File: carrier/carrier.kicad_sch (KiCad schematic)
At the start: 2 parts, among them J1 DF40GB-30DP-0.4V(51), U1 TC58NVG1S3HBAI6

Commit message: Rename project libraries to 'carrier' for consistency
lib/bga67-to-dip.kicad_sym -> lib/carrier.kicad_sym; nicknames now match
the directory names. Schematic instance lib_ids and U1's footprint field
updated. Both projects' lib tables rebuilt.

Co-Authored-By: Claude Opus 5 <noreply@anthropic.com>
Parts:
- J1: symbol bga67-to-dip:DF40GB-30DP-0.4V_51_ -> carrier:DF40GB-30DP-0.4V_51_
- U1: footprint bga67-to-dip:BGA-67_6.5x8.0mm_Layout8x10_P0.8mm -> carrier:BGA-67_6.5x8.0mm_Layout8x10_P0.8mm; symbol bga67-to-dip:TC58NVG1S3HBAI6 -> carrier:TC58NVG1S3HBAI6
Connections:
- net ALE: no longer J1.12, U1.B3 (ALE)
- net CLE: no longer J1.8, U1.C4 (CLE)
- net GND: no longer J1.10, J1.11, J1.14, J1.18, J1.2, J1.22, J1.23, J1.26, J1.27, J1.3, J1.30, J1.6, J1.7, J1.G1 (GND), J1.G2 (GND), J1.G3 (GND), J1.G4 (GND), U1.B4 (VSS), U1.J2 (VSS), U1.J7 (VSS)
- net IO1: no longer J1.1, U1.G3 (I/O1)
- net IO2: no longer J1.5, U1.H3 (I/O2)
- net IO3: no longer J1.9, U1.J3 (I/O3)
- net IO4: no longer J1.13, U1.J4 (I/O4)
- net IO5: no longer J1.17, U1.J5 (I/O5)
- net IO6: no longer J1.21, U1.H6 (I/O6)
- net IO7: no longer J1.25, U1.J6 (I/O7)
- net IO8: no longer J1.29, U1.H7 (I/O8)
- net RY//BY: no longer J1.28, U1.B7 (RY/~{BY})
- net VCC: no longer J1.15, J1.19, U1.G7 (VCC), U1.H5 (VCC)
- net /CE: no longer J1.4, U1.B5 (~{CE})
- net /RE: no longer J1.20, U1.C3 (~{RE})
- net /WE: no longer J1.16, U1.B6 (~{WE})
- net /WP: no longer J1.24, U1.B2 (~{WP})
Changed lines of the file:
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@@
 	)
 	(symbol
-		(lib_id "bga67-to-dip:DF40GB-30DP-0.4V_51_")
+		(lib_id "carrier:DF40GB-30DP-0.4V_51_")
 		(at 170.18 92.71 0)
 		(unit 1)
@@
 	)
 	(symbol
-		(lib_id "bga67-to-dip:TC58NVG1S3HBAI6")
+		(lib_id "carrier:TC58NVG1S3HBAI6")
 		(at 59.69 52.07 0)
 		(unit 1)
@@
 			)
 		)
-		(property "Footprint" "bga67-to-dip:BGA-67_6.5x8.0mm_Layout8x10_P0.8mm"
+		(property "Footprint" "carrier:BGA-67_6.5x8.0mm_Layout8x10_P0.8mm"
 			(at 59.69 52.07 0)
 			(hide yes)

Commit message: Fix stale library nickname in schematic symbol cache
The lib_symbols cache still keyed its three entries under the old
'bga67-to-dip:' nickname while the placed instances reference
'carrier:'. KiCad could not resolve the cached definitions, so U1 and
J1 were instantiated without pins: every wire endpoint and label came
up dangling and the netlist collapsed to 2 nets (all 67 U1 pads on one,
all 34 J1 pads on the other).

ERC 85 violations -> 2. The remaining two are power_pin_not_driven on
VCC/GND, which is expected on a board fed through a connector.

Netlist now exports 17 nets plus 47 NC singletons, and matches the ball
map and the connector table in docs/connector-pinout.md exactly.

Co-Authored-By: Claude Opus 5 <noreply@anthropic.com>
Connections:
- net ALE: now also J1.12, U1.B3 (ALE)
- net CLE: now also J1.8, U1.C4 (CLE)
- net GND: now also J1.10, J1.11, J1.14, J1.18, J1.2, J1.22, J1.23, J1.26, J1.27, J1.3, J1.30, J1.6, J1.7, J1.G1 (GND), J1.G2 (GND), J1.G3 (GND), J1.G4 (GND), U1.B4 (VSS), U1.J2 (VSS), U1.J7 (VSS)
- net IO1: now also J1.1, U1.G3 (I/O1)
- net IO2: now also J1.5, U1.H3 (I/O2)
- net IO3: now also J1.9, U1.J3 (I/O3)
- net IO4: now also J1.13, U1.J4 (I/O4)
- net IO5: now also J1.17, U1.J5 (I/O5)
- net IO6: now also J1.21, U1.H6 (I/O6)
- net IO7: now also J1.25, U1.J6 (I/O7)
- net IO8: now also J1.29, U1.H7 (I/O8)
- net RY//BY: now also J1.28, U1.B7 (RY/~{BY})
- net VCC: now also J1.15, J1.19, U1.G7 (VCC), U1.H5 (VCC)
- net /CE: now also J1.4, U1.B5 (~{CE})
- net /RE: now also J1.20, U1.C3 (~{RE})
- net /WE: now also J1.16, U1.B6 (~{WE})
- net /WP: now also J1.24, U1.B2 (~{WP})

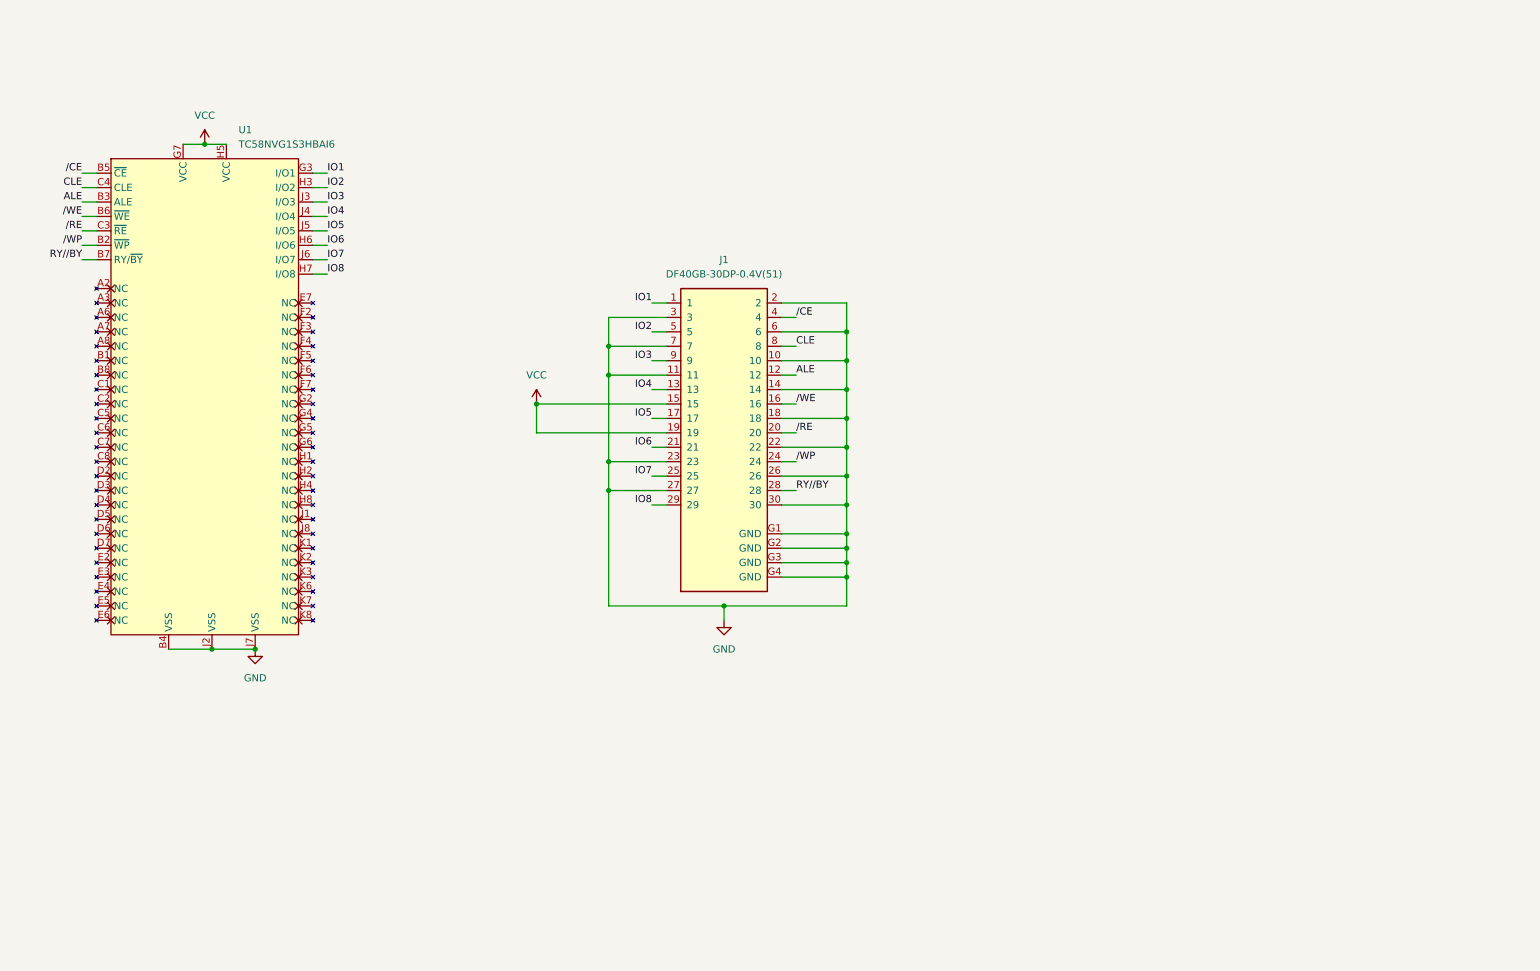
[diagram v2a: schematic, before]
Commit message: Re-derive the J1 pinout from ball geometry; regenerate both schematics
Alex asked to optimise J1's pin assignment for the BGA fanout, and to
consider routing on the inner layers working back from J1 rather than
out from U1. Working backwards is what produced the result.

The topology falls out of the ball map with no slack. The VFBGA67's 20
used balls split into an upper cluster (columns 2-4: IO1-IO4 plus
CLE/RE/ALE/WP) and a lower one (columns 5-7: IO5-IO8, CE/WE/RY-BY and
both VCC balls) - exactly 8 and 7 signals. J1's odd row has exactly 8
signal slots and its even row exactly 7. So the row assignment is
forced, and within a row ordering by ball x makes the escape fan out
monotonically. IO1-IO8 are no longer in pin order on the connector;
that is deliberate and safe, because the rule that matters is the
end-to-end mapping, not the connector order.

Measured against the previous pinout with a routing-aware cost model
(octilinear where clear, around-the-end where the connector body is in
the way): 141.2 mm -> 74.8 mm of point-to-point routing, IO skew
10.32 mm -> 2.94 mm, and around-the-end paths 11 -> 5. Constraining the
bus to stay contiguous recovers almost none of that (139.6 mm), because
the IO balls all sit on one side while a monotonic bus spans J1's full
5.6 mm.

Skew was not the reason to do this. 10 mm is ~62 ps on FR4 against a
25 ns read cycle. The win is copper length and via count.

tools/pinout.py is now the single source: it carries the table and a
checker for the checkerboard invariant (no signal adjacent to or
opposite another signal) and the net set. Both schematics were
generated from it. Verified: carrier ERC 0, base ERC 0, both J1s match
the table, U1 matches the datasheet ball map, J2 matches the TSOP48
map, and IOn traces ball -> J1 pin -> TSOP48 pin end to end.

Carrier PCB carries placement, net re-import and the BGA escape (20/20
balls, DRC 0 errors). The J1 fanout is NOT routed in this commit - see
the next commit message / handoff for w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
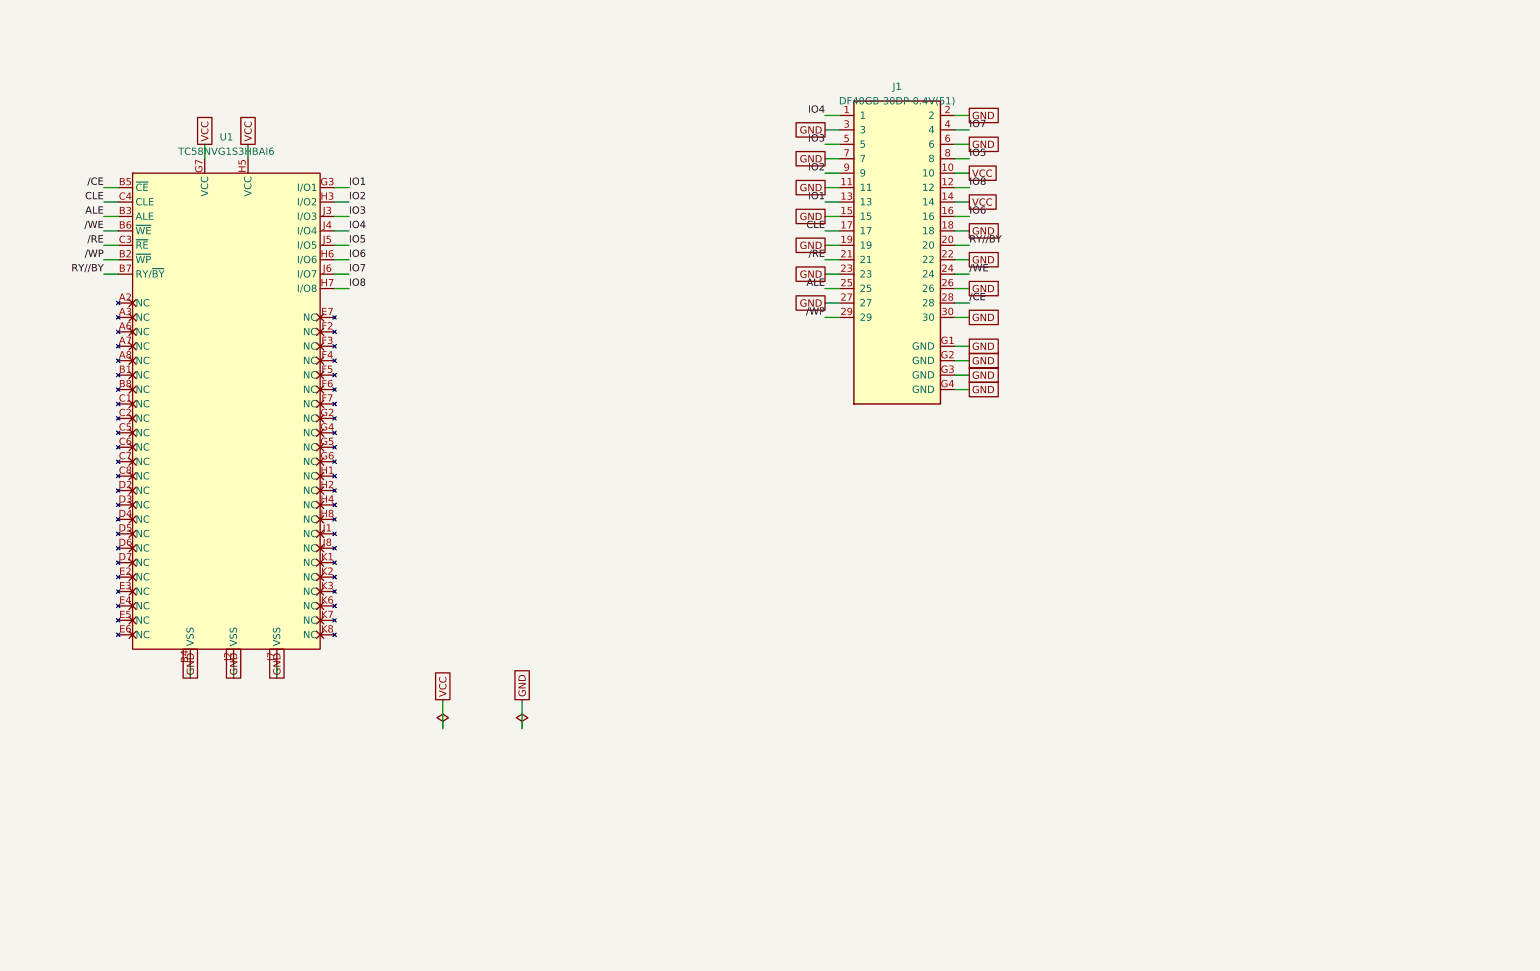
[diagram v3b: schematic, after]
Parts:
- U1: now in the parts list
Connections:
- net ALE: now also J1.25; no longer J1.12
- net CLE: now also J1.17; no longer J1.8
- net GND: now also J1.15, J1.19; no longer J1.10, J1.14
- net IO1: now also J1.13; no longer J1.1
- net IO2: now also J1.9; no longer J1.5
- net IO3: now also J1.5; no longer J1.9
- net IO4: now also J1.1; no longer J1.13
- net IO5: now also J1.8; no longer J1.17
- net IO6: now also J1.16; no longer J1.21
- net IO7: now also J1.4; no longer J1.25
- net IO8: now also J1.12; no longer J1.29
- net RY//BY: now also J1.20; no longer J1.28
- net VCC: now also J1.10, J1.14; no longer J1.15, J1.19
- net /CE: now also J1.28; no longer J1.4
- net /RE: now also J1.21; no longer J1.20
- net /WE: now also J1.24; no longer J1.16
- net /WP: now also J1.29; no longer J1.24
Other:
- title: VFBGA67 to Mezzanine -> VFBGA67 to DF40 Mezzanine

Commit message: Carrier fully routed; propagate the VCC pin move to base and the docs
Alex routed the carrier: 0 DRC violations, 0 unconnected, one via per
signal net (20 total), uniform 0.15 mm tracks, teardrops on every
via/pad transition, GND poured on all four layers.

While routing he moved VCC from J1 pin 14 to pin 6, which is the right
call - pin 6's x lines up with the VCC ball H5, and pin 10 already lined
up with G7. But the change landed on the carrier only, so pin 6 was VCC
on one board and GND on the other, and pin 14 the reverse. Mated, that
is VCC shorted to GND through two pins.

Neither project can catch this: they are separate KiCad projects, so
each one's ERC and DRC pass happily. This is exactly the failure the
"single source of truth" note in the pinout doc exists to prevent.

Adopted the carrier's version as canonical: tools/pinout.py now has
VCC on 6 and 10, base regenerated from it, doc table updated. The
checkerboard invariant still holds. Verified both J1s now agree on all
34 pins including the G tabs.

carrier ERC 0, base ERC 0, carrier DRC 0 violations / 0 unconnected.

Co-Authored-By: Claude Opus 5 <noreply@anthropic.com>
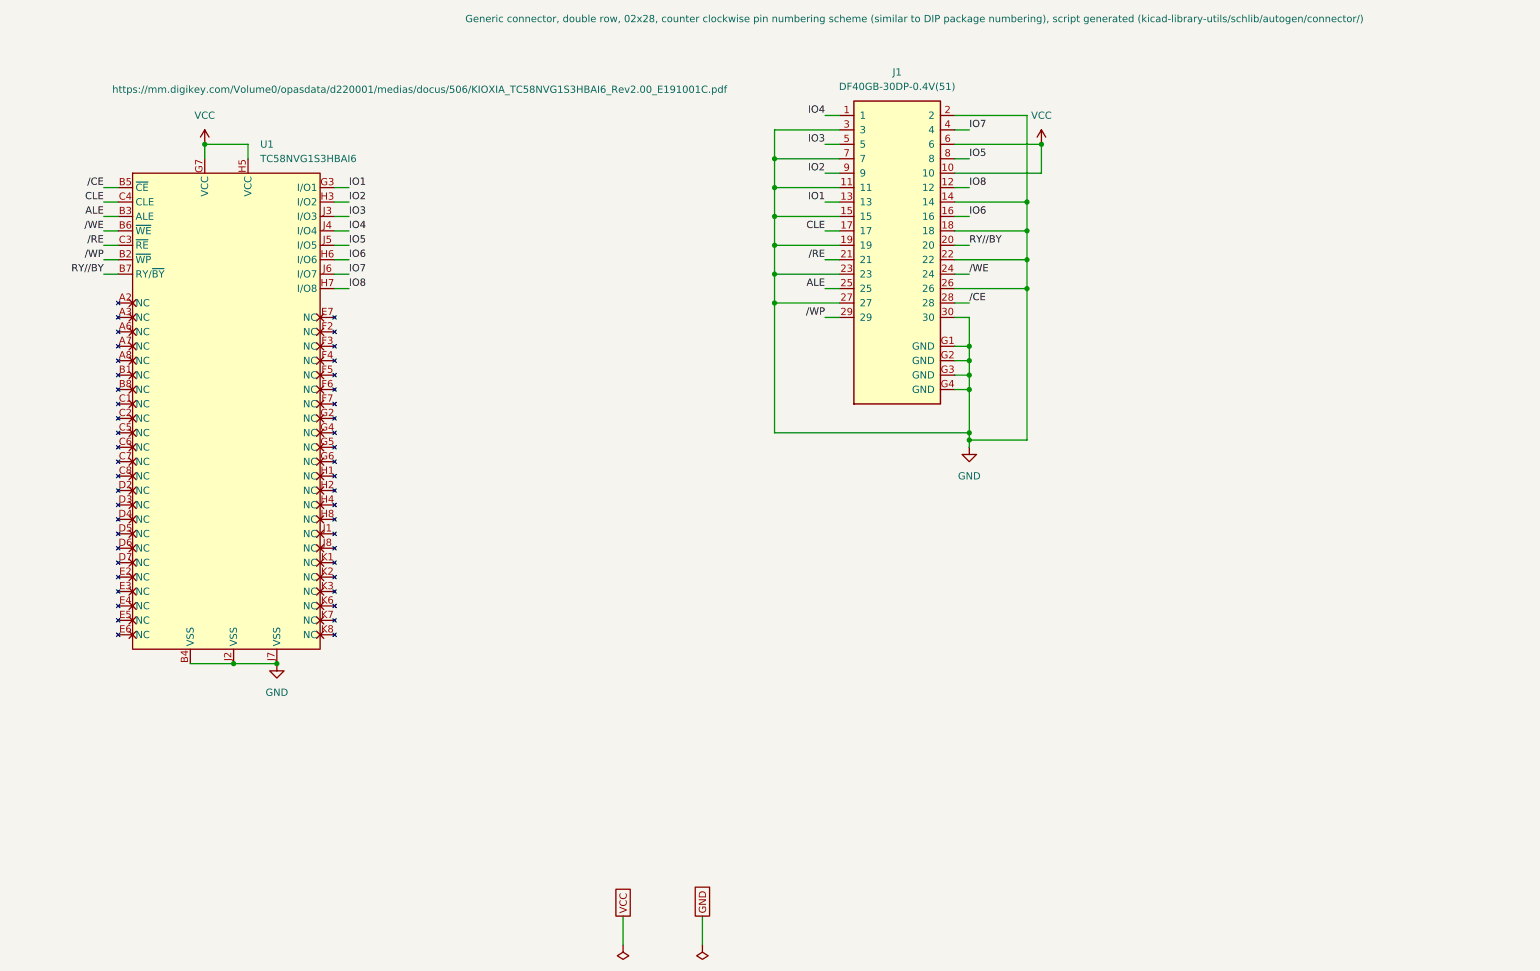
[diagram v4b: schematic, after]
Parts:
- U1: now left out of the parts list
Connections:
- net GND: now also J1.14; no longer J1.6
- net VCC: now also J1.6; no longer J1.14

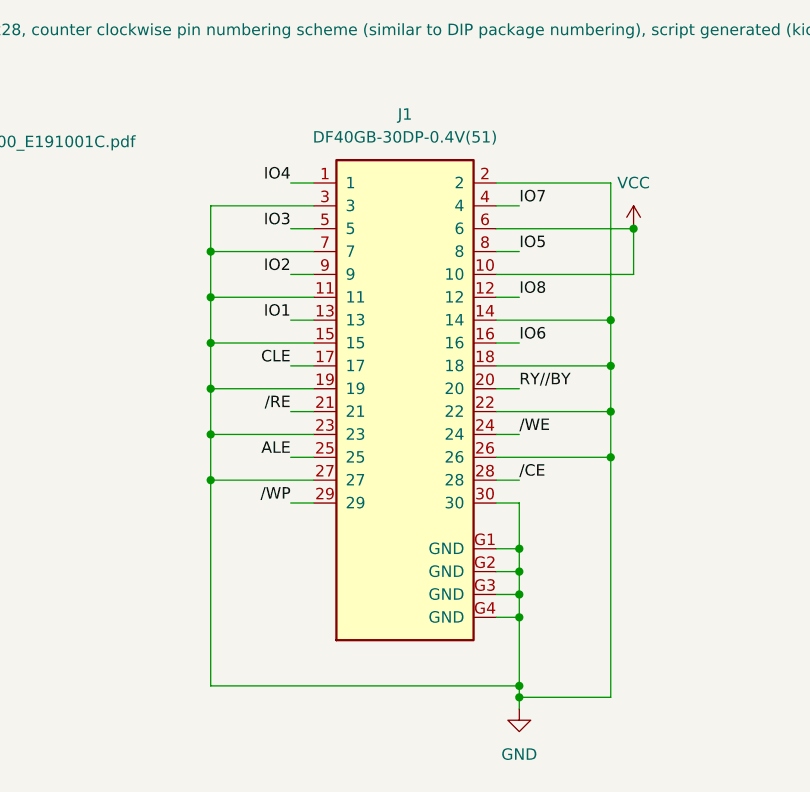
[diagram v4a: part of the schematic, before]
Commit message: Swap mezzanine to DF40TC 4.0mm; base DIP48 field goes surface-mount
The 1.5 mm DF40GB stack left no room under the base board and the
through-hole DIP48 socket put tails into the space the carrier occupies.
Both are now addressed by part choice rather than by moving anything.

Mezzanine, 1.5 mm -> 4.0 mm:
  carrier J1  DF40GB-30DP-0.4V(51)     -> DF40TC-30DP-0.4V(51)
  base    J1  DF40GB(1.5)-30DS-0.4V(51)-> DF40TC(4.0)-30DS-0.4V(51)

4.0 mm at 30 positions does not exist in any non-T DF40 family, but it is
mass production in DF40T (125 C, unshielded).  Verified against the
DF40T/DF40GT catalog (Jan 2026) p.2 variation matrix and p.8 combinations
table; 4.5-7.0 mm at 30 pos is still Under Planning, so 4.0 is the ceiling.
The plug carries no stacking height in its part number -- one DF40TC plug
serves 1.5 through 4.0 mm and the receptacle sets the gap.

The land patterns are the reason this is cheap: DF40T catalog p.9 gives the
plug as P=0.4, B=5.60, pad 0.23 wide, rows 3.37/2.05 -> 0.66 long at
y=+-1.355, and DF40 catalog p.10 (DF40HC, No Retention Tab) gives the
receptacle as pad 0.2 x 0.70 at y=+-1.54.  Both are bit-identical to the
DF40GB footprints already in the tree.  All 30 signal pads are unmoved on
both boards; only the four G1-G4 retention/shield tabs go away, because
DF40TC has none.  Verified pad-by-pad against the originals.

Costs of the DF40T family, for the record: 0.3 A instead of 0.5 A (the
flash draws 30 mA), 10 mating cycles instead of 30 (the carrier is the
joint that should stay mated), and no shield.

DIP48 field, through-hole -> surface mount:
  base J2  DIP-48_Socket_W15.24mm_P2.54mm
        -> DIP-48_SocketStrip_SMD_W15.24mm_P2.54mm
Two 1x24 SMT socket strips (Samtec SSM-124-L-SV class) on 15.24 mm
centres.  No one-piece SMT DIP48 at 0.6 in exists in distribution.  Tails
stagger +-1.65 mm about each row centreline, so all 48 pad Y coordinates
are unchanged and the row centres still sit where the adapter pins land;
the inner pad edges leave 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
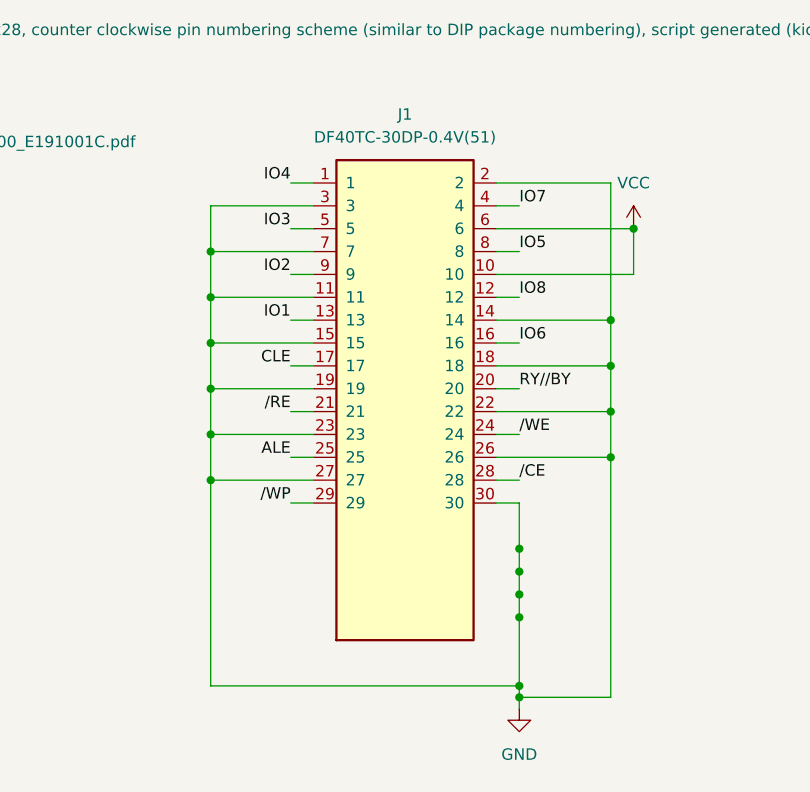
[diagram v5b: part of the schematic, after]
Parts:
- J1: value DF40GB-30DP-0.4V(51) -> DF40TC-30DP-0.4V(51); footprint Connector_Hirose_DF40:HIROSE_DF40GB-30DP-0.4V_51_ -> Connector_Hirose_DF40:HIROSE_DF40TC-30DP-0.4V_51_; symbol carrier:DF40GB-30DP-0.4V_51_ -> carrier:DF40TC-30DP-0.4V_51_
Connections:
- net GND: no longer J1.G1 (GND), J1.G2 (GND), J1.G3 (GND), J1.G4 (GND)
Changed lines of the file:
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@@
-	(wire
-		(pts
-			(xy 210.82 87.63) (xy 213.36 87.63)
-		)
-		(stroke
-			(width 0)
-			(type default)
-		)
-	)
 	(wire
 		(pts
@@
 	(wire
 		(pts
-			(xy 210.82 85.09) (xy 213.36 85.09)
-		)
-		(stroke
-			(width 0)
-			(type default)
-		)
-	)
-	(wire
-		(pts
 			(xy 179.07 64.77) (xy 190.5 64.77)
 		)
@@
 	(wire
 		(pts
-			(xy 210.82 90.17) (xy 213.36 90.17)
-		)
-		(stroke
-			(width 0)
-			(type default)
-		)
-	)
-	(wire
-		(pts
 			(xy 179.07 59.69) (xy 179.07 64.77)
-		)
-		(stroke
-			(width 0)
-			(type default)
-		)
-	)
-	(wire
-		(pts
-			(xy 210.82 82.55) (xy 213.36 82.55)
 		)
 		(stroke
@@
 	)
 	(symbol
-		(lib_id "carrier:DF40GB-30DP-0.4V_51_")
+		(lib_id "carrier:DF40TC-30DP-0.4V_51_")
 		(at 200.66 59.69 0)
 		(unit 1)
@@
 			)
 		)
-		(property "Value" "DF40GB-30DP-0.4V(51)"
+		(property "Value" "DF40TC-30DP-0.4V(51)"
 			(at 200.66 36.83 0)
 			(show_name no)
@@
 			)
 		)
-		(property "Footprint" "Connector_Hirose_DF40:HIROSE_DF40GB-30DP-0.4V_51_"
+		(property "Footprint" "Connector_Hirose_DF40:HIROSE_DF40TC-30DP-0.4V_51_"
 			(at 200.66 59.69 0)
 			(hide yes)
@@
 		(pin "30"
 		)
-		(pin "G1"
-		)
-		(pin "G2"
-		)
-		(pin "G3"
-		)
-		(pin "G4"
-		)
 		(instances
